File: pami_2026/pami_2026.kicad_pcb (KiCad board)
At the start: 4 copper layers, 57.8 x 50.2 mm, 75 parts, among them Q1 PMOS, Q2 PMOS, SW1 SW_Reed, U1 ESP32-WROOM-E, U2 AP63205WU, U3 DRV8871DDA, U5 AP63203WU, U6 DRV8871DDA

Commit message: Fixes and updates to v2
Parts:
- removed Q1, Q2: PMOS, Package_TO_SOT_SMD:SOT-223
- removed R1: 100K, Resistor_SMD:R_0603_1608Metric
- removed R20: 10K, Resistor_SMD:R_0603_1608Metric
- added S_5V1: RED LED, LED_SMD:LED_0603_1608Metric, F.Cu at (127.5, 86.8)
- moved C19 39.5 mm to (131.5, 107.0)
- moved D5 39.2 mm to (175.0, 95.5)
- moved C12 20.1 mm to (141.4, 81.7), turned to 90 degrees
- moved C4 19.9 mm to (128.0, 118.5), turned to 90 degrees
- moved C10 17.2 mm to (139.5, 81.7)
- moved C9 17.2 mm to (140.0, 98.0)
- moved R7 17.2 mm to (140.0, 99.6)
- moved L1 16.9 mm to (131.5, 121.0), turned to -90 degrees
- moved L2 15.3 mm to (140.0, 121.0), turned to -90 degrees
- moved C8 14.7 mm to (136.5, 118.5), turned to 90 degrees
- moved C7 14.6 mm to (141.5, 113.0), turned to 0 degrees
- moved C5 14.0 mm to (133.1, 113.0)
- moved C2 10.8 mm to (136.5, 115.0), turned to -90 degrees
- moved C3 10.1 mm to (128.0, 115.0), turned to -90 degrees
- moved U2 10.1 mm to (139.6, 116.4), turned to -90 degrees
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- renumbered S_5V1 to S_5V2
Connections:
- net BATTERY_LEVEL renamed /Microcontroller/BATTERY_LEVEL
- net BOOT renamed /Microcontroller/BOOT
- net DC_A1 renamed /Actuators, Sensors, Utility/DC_A1
- net DC_A2 renamed /Actuators, Sensors, Utility/DC_A2
- net DC_B1 renamed /Actuators, Sensors, Utility/DC_B1
- net DC_B2 renamed /Actuators, Sensors, Utility/DC_B2
- net DC_OUT_A+ renamed /Actuators, Sensors, Utility/DC_OUT_A+
- net DC_OUT_A- renamed /Actuators, Sensors, Utility/DC_OUT_A-
- net DC_OUT_B+ renamed /Actuators, Sensors, Utility/DC_OUT_B+
- net DC_OUT_B- renamed /Actuators, Sensors, Utility/DC_OUT_B-
- net HALL_A1 renamed /Actuators, Sensors, Utility/HALL_A1
- net HALL_A2 renamed /Actuators, Sensors, Utility/HALL_A2
- net HALL_B1 renamed /Actuators, Sensors, Utility/HALL_B1
- net HALL_B2 renamed /Actuators, Sensors, Utility/HALL_B2
- net RST renamed /Microcontroller/RST
- net SERVO_1 renamed /Microcontroller/SERVO_1
- net SERVO_2 renamed /Microcontroller/SERVO_2
- net SW_Team renamed /Microcontroller/SW_Team
- net SW_Tirette renamed /Microcontroller/SW_Tirette
- net TEAM_RGB renamed /Microcontroller/TEAM_RGB
- net UART_RX renamed /Microcontroller/UART_RX
- net UART_TX renamed /Microcontroller/UART_TX
- net US_RX renamed /Microcontroller/US_RX
- net US_TX renamed /Microcontroller/US_TX
- C1 pad 1: Net-(U5-SW) -> Net-(U5-BST)
- C1 pad 2: Net-(U5-BST) -> Net-(U5-SW)
- C3 pad 1: Net-(D5-K) -> BATT
- C6 pad 1: Net-(U2-SW) -> Net-(U2-BST)
- C6 pad 2: Net-(U2-BST) -> Net-(U2-SW)
- D1 pad 2: Net-(D1-A+) -> GND
- D5 pad 1: Net-(D5-K) -> BATT
- F1 pad 2: Net-(Q1-D) -> BATT
- L1 pad 1: Net-(U5-BST) -> Net-(U5-SW)
- L2 pad 1: Net-(U2-BST) -> Net-(U2-SW)
- U5 pad 2: Net-(D5-K) -> BATT
- U5 pad 3: Net-(D5-K) -> BATT
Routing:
- net EXTERNAL: track 58.1 -> 4.18 mm
- net GND: track 96.1 -> 75.2 mm, vias 123 -> 175
- net Net-(D1-A+): track 17.7 -> 0.00 mm
- net Net-(D5-K): track 15.9 -> 0.00 mm
- net Net-(BAU1-Pin_1): track 3.15 -> 17.2 mm
- net Net-(Q1-D): track 13.6 -> 0.00 mm, vias 2 -> 0
- net +3.3V: track 84.2 -> 97.4 mm
- net Net-(U5-BST): track 15.5 -> 2.43 mm
- net Net-(U2-BST): track 15.6 -> 2.53 mm
- net BATT: track 146.8 -> 154.5 mm, vias 14 -> 9
- net +5V: track 106.4 -> 113.8 mm, vias 4 -> 3
- net /Microcontroller/RST: track 24.2 -> 31.0 mm, vias 0 -> 2
- net Net-(U5-SW): track 2.17 -> 5.56 mm
- net Net-(U2-SW): track 2.18 -> 5.33 mm
- net /Actuators, Sensors, Utility/HALL_B1: track 36.8 -> 35.1 mm
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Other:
- board text added: "Cartes PAMIs 2026 V2"
- board text removed: "Cartes PAMIs 2026 V1"
- board text removed: "U3"
- board text removed: "U6"

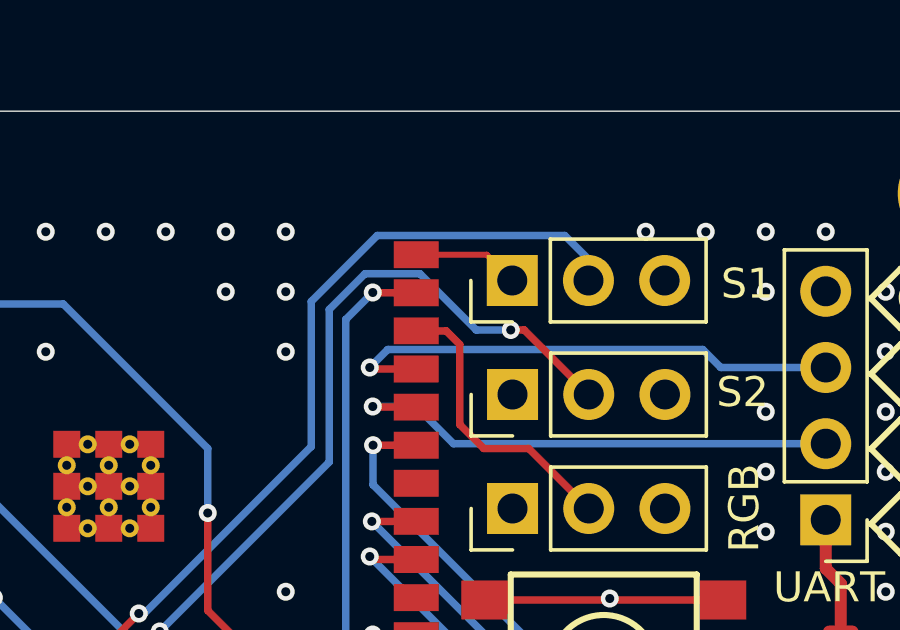
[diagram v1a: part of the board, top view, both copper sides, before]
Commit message: Fix servo pinout
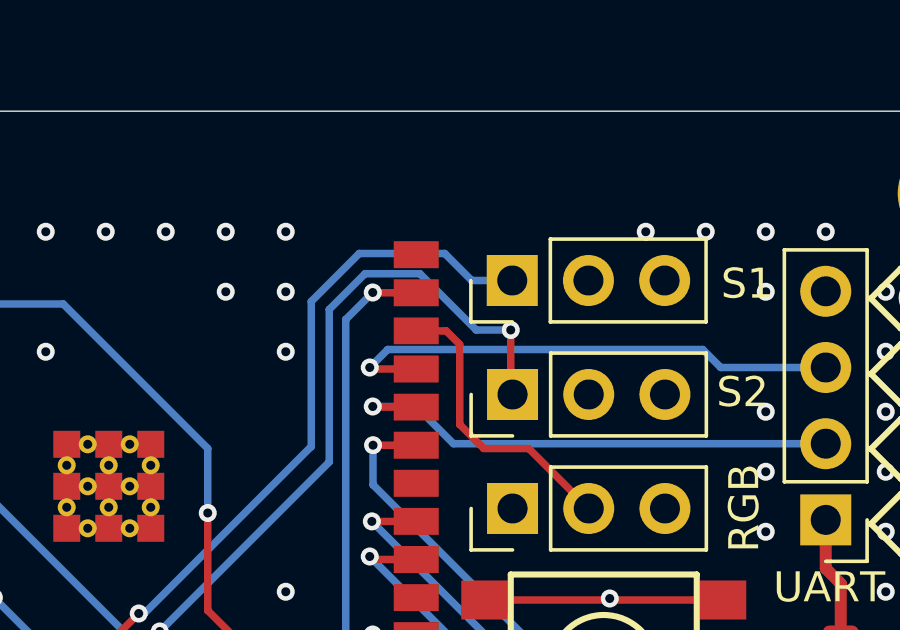
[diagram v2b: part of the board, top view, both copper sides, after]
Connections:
- SERVO_1 pad 1: GND -> /Microcontroller/SERVO_1
- SERVO_1 pad 2: /Microcontroller/SERVO_1 -> +5V
- SERVO_1 pad 3: +5V -> GND
- SERVO_2 pad 1: GND -> /Microcontroller/SERVO_2
- SERVO_2 pad 2: /Microcontroller/SERVO_2 -> +5V
- SERVO_2 pad 3: +5V -> GND
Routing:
- net GND: track 75.2 -> 71.7 mm, vias 175 -> 174
- net /Microcontroller/SERVO_1: track 32.6 -> 29.2 mm
- net +5V: track 113.8 -> 110.4 mm
- net /Microcontroller/SERVO_2: track 33.4 -> 32.1 mm
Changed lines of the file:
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@@
 			(layers "*.Cu" "*.Mask")
 			(remove_unused_layers no)
-			(net 4 "GND")
+			(net 42 "/Microcontroller/SERVO_2")
 			(pinfunction "Pin_1")
 			(pintype "passive")
@@
 			(layers "*.Cu" "*.Mask")
 			(remove_unused_layers no)
-			(net 42 "/Microcontroller/SERVO_2")
+			(net 8 "+5V")
 			(pinfunction "Pin_2")
 			(pintype "passive")
@@
 			(layers "*.Cu" "*.Mask")
 			(remove_unused_layers no)
-			(net 8 "+5V")
+			(net 4 "GND")
 			(pinfunction "Pin_3")
 			(pintype "passive")
@@
 			(layers "*.Cu" "*.Mask")
 			(remove_unused_layers no)
-			(net 4 "GND")
+			(net 41 "/Microcontroller/SERVO_1")
 			(pinfunction "Pin_1")
 			(pintype "passive")
@@
 			(layers "*.Cu" "*.Mask")
 			(remove_unused_layers no)
-			(net 41 "/Microcontroller/SERVO_1")
+			(net 8 "+5V")
 			(pinfunction "Pin_2")
 			(pintype "passive")
@@
 			(layers "*.Cu" "*.Mask")
 			(remove_unused_layers no)
-			(net 8 "+5V")
+			(net 4 "GND")
 			(pinfunction "Pin_3")
 			(pintype "passive")
@@
 	)
 	(segment
-		(start 163.2 81.04)
-		(end 164.06 81.9)
-		(width 0.2)
-		(layer "F.Cu")
-		(net 4)
-	)
-	(segment
 		(start 129.9 81.2125)
 		(end 136.825 81.2125)
@@
 	)
 	(segment
-		(start 160.85 81.04)
-		(end 163.2 81.04)
-		(width 0.2)
-		(layer "F.Cu")
-		(net 4)
-	)
-	(segment
 		(start 175.625 121.8)
 		(end 175.625 117.8)
@@
 	)
 	(via
-		(at 164.05 81.9)
-		(size 0.6)
-		(drill 0.3)
-		(layers "F.Cu" "B.Cu")
-		(net 4)
-	)
-	(via
 		(at 124.5 112.275)
 		(size 0.6)
@@
 	)
 	(segment
-		(start 164.06 89.5)
-		(end 164.06 88.34)
+		(start 166.6 81.91)
+		(end 166.59 81.9)
 		(width 0.8)
 		(layer "In2.Cu")
@@
 	)
 	(segment
-		(start 164.8 87.6)
-		(end 168.8 87.6)
+		(start 166.6 86.96)
+		(end 166.6 85.7)
+		(width 0.8)
+		(layer "In2.Cu")
+		(net 8)
+	)
+	(segment
+		(start 164.06 89.5)
+		(end 166.6 86.96)
 		(width 0.8)
 		(layer "In2.Cu")
@@
 	)
 	(segment
-		(start 157.1 88.6)
-		(end 163.16 88.6)
-		(width 0.8)
-		(layer "In2.Cu")
-		(net 8)
-	)
-	(segment
-		(start 135.3865 85.3135)
-		(end 138.7 82)
+		(start 166.6 85.7)
+		(end 166.6 81.91)
 		(width 0.8)
 		(layer "In2.Cu")
@@
 	)
 	(segment
-		(start 164.06 88.34)
-		(end 164.8 87.6)
-		(width 0.8)
-		(layer "In2.Cu")
-		(net 8)
-	)
-	(segment
-		(start 168.8 87.6)
-		(end 169.14 87.26)
+		(start 157.1 88.6)
+		(end 163.16 88.6)
 		(width 0.8)
 		(layer "In2.Cu")
@@
 	)
 	(segment
-		(start 169.14 81.9)
-		(end 169.14 85.7)
+		(start 135.3865 85.3135)
+		(end 138.7 82)
 		(width 0.8)
 		(layer "In2.Cu")
@@
 	)
 	(segment
-		(start 169.14 87.26)
-		(end 169.14 85.7)
-		(width 0.8)
-		(layer "In2.Cu")
-		(net 8)
-	)
-	(segment
 		(start 148.307107 102.5)
 		(end 147 102.5)
@@
 	)
 	(segment
-		(start 166.6 81.2)
-		(end 166.6 81.9)
+		(start 161.8 81)
+		(end 162.7 81.9)
 		(width 0.25)
 		(layer "B.Cu")
@@
 	)
 	(segment
-		(start 151.785298 93)
-		(end 157.35 87.435298)
+		(start 162.7 81.9)
+		(end 164.05 81.9)
 		(width 0.25)
 		(layer "B.Cu")
@@
 	)
 	(segment
-		(start 165.8 80.4)
-		(end 166.6 81.2)
+		(start 157.35 87.435298)
+		(end 157.35 82.6)
 		(width 0.25)
 		(layer "B.Cu")
@@
 	)
 	(segment
-		(start 157.35 87.435298)
-		(end 157.35 82.6)
+		(start 158.95 81)
+		(end 161.8 81)
 		(width 0.25)
 		(layer "B.Cu")
@@
 	)
 	(segment
-		(start 159.55 80.4)
-		(end 165.8 80.4)
+		(start 151.6 93)
+		(end 151.785298 93)
 		(width 0.25)
 		(layer "B.Cu")
@@
 	)
 	(segment
-		(start 151.6 93)
-		(end 151.785298 93)
+		(start 151.785298 93)
+		(end 157.35 87.435298)
 		(width 0.25)
 		(layer "B.Cu")
@@
 	(segment
 		(start 157.35 82.6)
-		(end 159.55 80.4)
+		(end 158.95 81)
 		(width 0.25)
 		(layer "B.Cu")
@@
 	)
 	(segment
-		(start 143.35 95.01)
-		(end 145.49 95.01)
+		(start 164 83.55)
+		(end 164 85.64)
 		(width 0.25)
 		(layer "F.Cu")
@@
 	)
 	(segment
-		(start 145.49 95.01)
-		(end 150.89 95.01)
+		(start 143.35 95.01)
+		(end 145.49 95.01)
 		(width 0.25)
 		(layer "F.Cu")
@@
 	)
 	(segment
-		(start 164 83.55)
-		(end 164.45 83.55)
+		(start 145.49 95.01)
+		(end 150.89 95.01)
 		(width 0.25)
 		(layer "F.Cu")
@@
 	)
 	(segment
-		(start 164.45 83.55)
-		(end 166.6 85.7)
+		(start 164 85.64)
+		(end 164.06 85.7)
 		(width 0.25)
 		(layer "F.Cu")
@@
 	)
 	(via
-		(at 164 83.55)
+		(at 152.3 93.6)
 		(size 0.6)
 		(drill 0.3)
@@
 	)
 	(via
-		(at 152.3 93.6)
+		(at 164 83.55)
 		(size 0.6)
 		(drill 0.3)
